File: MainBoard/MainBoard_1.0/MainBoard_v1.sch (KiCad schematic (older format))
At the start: 165 parts, among them J1 ILG, J10 SH, J11 SH, J12 SH, J13 FFC, J14 SH, J2 SH, J3 SH, J4 PA, J5 Micro_SD_Card_Det_Hirose_DM3AT, J6 SH, J7 ENC, J8 ENC, J9 PA, Q1 AON7400B, Q10 IRLML6344, Q2 AON7400B, Q3 AON7400B, Q4 AON7400B, Q5 AON7400B, Q6 AON7400B, Q7 2N7002K, Q8 AON7400B, Q9 AON7400B, SW1 SKRPACE010, SW2 SSSS213202, SW3 FR01SC16P-S, SW4 SKRHAAE010, U1 SI7469DP-T1-GE3, U10 DRV8701E, U11 MMC5983MA, U2 LT1963A-TSSOP, U3 TPS62143, U4 ECS-2520S33, U5 INA260, U6 DRV8701E, U7 ICM20648, U8 STM32F469VG, U9 INA260

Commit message: ver_2021
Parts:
- C2, C28, C44: symbol Device:CP_Small -> MainBoard_v1-rescue:CP_Small-Device
- D1, D7: symbol Device:D_Schottky_Small_ALT -> MainBoard_v1-rescue:D_Schottky_Small_ALT-Device
- D2, D3: symbol Device:D_Zener_Small_ALT -> MainBoard_v1-rescue:D_Zener_Small_ALT-Device
- D4, D5, D6, D8, D9: symbol Device:LED_Small_ALT -> MainBoard_v1-rescue:LED_Small_ALT-Device
- FB1, FB2, FB3, FB4, FB5, FB6, FB7: symbol Device:Ferrite_Bead_Small -> MainBoard_v1-rescue:Ferrite_Bead_Small-Device
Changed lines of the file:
@@
 $EndComp
 $Comp
-L Device:CP_Small C2
+L MainBoard_v1-rescue:CP_Small-Device C2
 U 1 1 5EC9A733
 P 7750 1700
@@
 	12850 1050 12850 1200
 $Comp
-L Device:D_Zener_Small_ALT D3
+L MainBoard_v1-rescue:D_Zener_Small_ALT-Device D3
 U 1 1 5ECD6403
 P 12600 1700
@@
 $EndComp
 $Comp
-L Device:D_Zener_Small_ALT D2
+L MainBoard_v1-rescue:D_Zener_Small_ALT-Device D2
 U 1 1 5ECD7671
 P 8900 1700
@@
 	8900 1800 8900 2150
 $Comp
-L Device:D_Schottky_Small_ALT D1
+L MainBoard_v1-rescue:D_Schottky_Small_ALT-Device D1
 U 1 1 5ECDC58D
 P 8750 1200
@@
 Connection ~ 1300 4500
 $Comp
-L Device:Ferrite_Bead_Small FB1
+L MainBoard_v1-rescue:Ferrite_Bead_Small-Device FB1
 U 1 1 5ECC6524
 P 1000 5700
@@
 $EndComp
 $Comp
-L Device:LED_Small_ALT D4
+L MainBoard_v1-rescue:LED_Small_ALT-Device D4
 U 1 1 5ECAB4EE
 P 8450 1850
@@
 $EndComp
 $Comp
-L Device:LED_Small_ALT D5
+L MainBoard_v1-rescue:LED_Small_ALT-Device D5
 U 1 1 5ECEEE7F
 P 12850 1850
@@
 $EndComp
 $Comp
-L Device:LED_Small_ALT D6
+L MainBoard_v1-rescue:LED_Small_ALT-Device D6
 U 1 1 5ED0949D
 P 15750 1850
@@
 Connection ~ 2000 8100
 $Comp
-L Device:D_Schottky_Small_ALT D7
+L MainBoard_v1-rescue:D_Schottky_Small_ALT-Device D7
 U 1 1 5F19FBEA
 P 1650 7400
@@
 	8550 6800 8550 7050
 $Comp
-L Device:Ferrite_Bead_Small FB2
+L MainBoard_v1-rescue:Ferrite_Bead_Small-Device FB2
 U 1 1 60318787
 P 6850 5900
@@
 $EndComp
 $Comp
-L Device:Ferrite_Bead_Small FB3
+L MainBoard_v1-rescue:Ferrite_Bead_Small-Device FB3
 U 1 1 60368094
 P 6850 6000
@@
 $EndComp
 $Comp
-L Device:Ferrite_Bead_Small FB4
+L MainBoard_v1-rescue:Ferrite_Bead_Small-Device FB4
 U 1 1 603B73FE
 P 6850 6100
@@
 $EndComp
 $Comp
-L Device:Ferrite_Bead_Small FB5
+L MainBoard_v1-rescue:Ferrite_Bead_Small-Device FB5
 U 1 1 60406759
 P 6850 6300
@@
 $EndComp
 $Comp
-L Device:Ferrite_Bead_Small FB6
+L MainBoard_v1-rescue:Ferrite_Bead_Small-Device FB6
 U 1 1 60455AD2
 P 6850 6500
@@
 $EndComp
 $Comp
-L Device:Ferrite_Bead_Small FB7
+L MainBoard_v1-rescue:Ferrite_Bead_Small-Device FB7
 U 1 1 604A4F68
 P 6850 6600
@@
 	9800 11000 10450 11000
 $Comp
-L Device:CP_Small C28
+L MainBoard_v1-rescue:CP_Small-Device C28
 U 1 1 67BA8F60
 P 14300 5400
@@
 	14300 5200 14300 5300
 $Comp
-L Device:CP_Small C44
+L MainBoard_v1-rescue:CP_Small-Device C44
 U 1 1 6806CE8E
 P 14150 9150
@@
 Wire Wire Line
 	6300 9200 6300 9250
-Text GLabel 6250 9900 0    50   Input ~ 0
-EXTRA1
 Text GLabel 6250 10000 0    50   Input ~ 0
+EXTRA1
+Text GLabel 6250 9900 0    50   Input ~ 0
 EXTRA2
 $Comp
@@
 	3400 10000 3400 10100
 $Comp
-L Device:LED_Small_ALT D8
+L MainBoard_v1-rescue:LED_Small_ALT-Device D8
 U 1 1 61039744
 P 1150 10550
@@
 $EndComp
 $Comp
-L Device:LED_Small_ALT D9
+L MainBoard_v1-rescue:LED_Small_ALT-Device D9
 U 1 1 6103974A
 P 1450 10550

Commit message: fixed right bottom
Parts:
- removed J3: SH, Connectors_JST:JST_SH_BM06B-SRSS-TB_06x1.00mm_Straight, symbol Connector_Generic:Conn_01x06
- added J3: STDC14, Connector_PinHeader_1.27mm:PinHeader_2x07_P1.27mm_Vertical_SMD, symbol Connector_Generic:Conn_02x07_Odd_Even
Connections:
- net +3V3: now also J3.3 (Pin_3)
- net ESC1_PWM: now also U8.99 (PB9); no longer U8.94 (PB5)
- net ESC2_PWM: now also U8.98 (PB8); no longer U8.93 (PB4)
- net ESC3_PWM: now also U8.94 (PB5); no longer U8.98 (PB8)
- net ESC4_PWM: now also U8.93 (PB4); no longer U8.99 (PB9)
- net GND: now also U7.11 (FSYNC), J3.11 (Pin_11), J3.5 (Pin_5), J3.7 (Pin_7)
- net NRST: now also J3.12 (Pin_12)
- net R_SW1: now also U8.85 (PD1); no longer U8.35 (PE10)
- net R_SW2: now also U8.87 (PD3); no longer U8.33 (PE8)
- net R_SW4: now also U8.88 (PD4); no longer U8.32 (PE7)
- net R_SW8: now also U8.91 (PD7); no longer U8.31 (PB2)
- net SW1: now also U8.31 (PB2); no longer U8.91 (PD7)
- net SW2: now also U8.32 (PE7); no longer U8.88 (PD4)
- net SW3: now also U8.33 (PE8); no longer U8.87 (PD3)
- net SW4: now also U8.35 (PE10); no longer U8.85 (PD1)
- net SWCLK: now also J3.6 (Pin_6)
- net SWDIO: now also J3.4 (Pin_4)
- net SWO: now also J3.8 (Pin_8)
- no-connect marks 46 -> 51
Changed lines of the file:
@@
 $EndComp
 $Comp
-L MainBoard_v1-rescue:ICM20648-shimoharu_library U7
-U 1 1 5EC2BB3D
-P 7750 4450
-F 0 "U7" V 8900 3400 50  0000 L CNN
-F 1 "ICM20648" V 8800 3150 50  0000 L CNN
-F 2 "Footprint:ICM20648" H 7750 4450 50  0001 C CNN
-F 3 "" H 7750 4450 50  0001 C CNN
-	1    7750 4450
-	0    -1   -1   0
-$EndComp
-$Comp
 L Connector_Generic:Conn_01x02 J1
 U 1 1 5EC51A22
@@
 Wire Wire Line
 	1300 4700 2050 4700
-Text GLabel 3050 6900 3    50   Input ~ 0
+Text GLabel 3450 3500 1    50   Input ~ 0
 R_SW8
-Text GLabel 3150 6900 3    50   Input ~ 0
+Text GLabel 3750 3500 1    50   Input ~ 0
 R_SW4
-Text GLabel 3250 6900 3    50   Input ~ 0
+Text GLabel 3850 3500 1    50   Input ~ 0
 R_SW2
-Text GLabel 3450 6900 3    50   Input ~ 0
+Text GLabel 4050 3500 1    50   Input ~ 0
 R_SW1
 Text GLabel 2050 5100 0    50   Input ~ 0
@@
 Text GLabel 4150 3500 1    50   Input ~ 0
 SW5
-Text GLabel 4050 3500 1    50   Input ~ 0
+Text GLabel 3450 6900 3    50   Input ~ 0
 SW4
-Text GLabel 3850 3500 1    50   Input ~ 0
+Text GLabel 3250 6900 3    50   Input ~ 0
 SW3
-Text GLabel 3750 3500 1    50   Input ~ 0
+Text GLabel 3150 6900 3    50   Input ~ 0
 SW2
 Text GLabel 3650 3500 1    50   Input ~ 0
@@
 Text GLabel 3550 3500 1    50   Input ~ 0
 USART_RX
-Text GLabel 3450 3500 1    50   Input ~ 0
+Text GLabel 3050 6900 3    50   Input ~ 0
 SW1
-Text GLabel 3150 3500 1    50   Input ~ 0
+Text GLabel 2650 3500 1    50   Input ~ 0
 ESC1_PWM
-Text GLabel 3250 3500 1    50   Input ~ 0
+Text GLabel 2750 3500 1    50   Input ~ 0
 ESC2_PWM
 Text GLabel 3050 3500 1    50   Input ~ 0
@@
 Wire Wire Line
 	2850 2900 2850 3500
-Text GLabel 2750 3500 1    50   Input ~ 0
-ESC3_PWM
-Text GLabel 2650 3500 1    50   Input ~ 0
+Text GLabel 3250 3500 1    50   Input ~ 0
 ESC4_PWM
+Text GLabel 3150 3500 1    50   Input ~ 0
+ESC3_PWM
 Text GLabel 3950 6900 3    50   Input ~ 0
 EXTRA2
@@
 Connection ~ 3150 1900
 $Comp
-L Connector_Generic:Conn_01x06 J3
-U 1 1 5ED71E7C
-P 4800 1350
-F 0 "J3" H 4880 1342 50  0000 L CNN
-F 1 "SH" H 4880 1251 50  0000 L CNN
-F 2 "Connectors_JST:JST_SH_BM06B-SRSS-TB_06x1.00mm_Straight" H 4800 1350 50  0001 C CNN
-F 3 "~" H 4800 1350 50  0001 C CNN
-	1    4800 1350
-	1    0    0    -1
-$EndComp
-$Comp
 L Connector_Generic:Conn_01x04 J2
 U 1 1 5ED7299E
@@
 L power:+3.3V #PWR03
 U 1 1 5ED95FDD
-P 4600 850
-F 0 "#PWR03" H 4600 700 50  0001 C CNN
-F 1 "+3.3V" H 4615 1023 50  0000 C CNN
-F 2 "" H 4600 850 50  0001 C CNN
-F 3 "" H 4600 850 50  0001 C CNN
-	1    4600 850
+P 4300 950
+F 0 "#PWR03" H 4300 800 50  0001 C CNN
+F 1 "+3.3V" H 4315 1123 50  0000 C CNN
+F 2 "" H 4300 950 50  0001 C CNN
+F 3 "" H 4300 950 50  0001 C CNN
+	1    4300 950
 	-1   0    0    -1
 $EndComp
 Wire Wire Line
-	4600 850  4600 1150
+	4300 950  4300 1250
 $Comp
 L power:GND #PWR010
 U 1 1 5EDA1506
-P 4200 2050
-F 0 "#PWR010" H 4200 1800 50  0001 C CNN
-F 1 "GND" H 4205 1877 50  0000 C CNN
-F 2 "" H 4200 2050 50  0001 C CNN
-F 3 "" H 4200 2050 50  0001 C CNN
-	1    4200 2050
+P 4100 1750
+F 0 "#PWR010" H 4100 1500 50  0001 C CNN
+F 1 "GND" H 4105 1577 50  0000 C CNN
+F 2 "" H 4100 1750 50  0001 C CNN
+F 3 "" H 4100 1750 50  0001 C CNN
+	1    4100 1750
 	1    0    0    -1
 $EndComp
-Wire Wire Line
-	4200 2050 4200 1350
 $Comp
 L power:+3.3V #PWR04
@@
 Wire Wire Line
 	5750 2000 5750 1450
-Text GLabel 4600 1250 0    50   Input ~ 0
-SWCLK
-Text GLabel 4600 1450 0    50   Input ~ 0
+Text GLabel 4950 1250 2    50   Input ~ 0
 SWDIO
-Text GLabel 4600 1550 0    50   Input ~ 0
+Text GLabel 4950 1650 2    50   Input ~ 0
 NRST
-Text GLabel 4600 1650 0    50   Input ~ 0
+Text GLabel 4950 1450 2    50   Input ~ 0
 SWO
-Wire Wire Line
-	4200 1350 4600 1350
 Text GLabel 5750 1250 0    50   Input ~ 0
 USART_RX
@@
 	7150 3800 7150 3050
 NoConn ~ 8850 3700
-NoConn ~ 8850 3800
 NoConn ~ 7950 3200
 NoConn ~ 8050 3200
@@
 	7500 4300 7500 4800
 Wire Wire Line
-	7500 4800 8900 4800
-Wire Wire Line
 	8900 4800 8900 4000
 Wire Wire Line
@@
 Wire Wire Line
 	6600 4300 7500 4300
+Wire Wire Line
+	7500 4800 8900 4800
+$Comp
+L MainBoard_v1-rescue:ICM20648-shimoharu_library U7
+U 1 1 5EC2BB3D
+P 7750 4450
+F 0 "U7" V 8900 3400 50  0000 L CNN
+F 1 "ICM20648" V 8800 3150 50  0000 L CNN
+F 2 "Footprint:ICM20648" H 7750 4450 50  0001 C CNN
+F 3 "" H 7750 4450 50  0001 C CNN
+	1    7750 4450
+	0    -1   -1   0
+$EndComp
+Wire Wire Line
+	8850 3800 9400 3800
+Wire Wire Line
+	9400 3800 9400 3900
+Connection ~ 9400 3900
+Text GLabel 4950 1350 2    50   Input ~ 0
+SWCLK
+NoConn ~ 4450 1150
+NoConn ~ 4950 1150
+Wire Wire Line
+	4300 1250 4450 1250
+Wire Wire Line
+	4100 1750 4100 1650
+Wire Wire Line
+	4100 1350 4450 1350
+$Comp
+L Connector_Generic:Conn_02x07_Odd_Even J3
+U 1 1 60D502E8
+P 4650 1450
+F 0 "J3" H 4700 1967 50  0000 C CNN
+F 1 "STDC14" H 4700 1876 50  0000 C CNN
+F 2 "Connector_PinHeader_1.27mm:PinHeader_2x07_P1.27mm_Vertical_SMD" H 4650 1450 50  0001 C CNN
+F 3 "~" H 4650 1450 50  0001 C CNN
+	1    4650 1450
+	1    0    0    -1
+$EndComp
+Wire Wire Line
+	4450 1450 4100 1450
+Connection ~ 4100 1450
+Wire Wire Line
+	4100 1450 4100 1350
+NoConn ~ 4450 1550
+NoConn ~ 4950 1550
+Wire Wire Line
+	4450 1650 4100 1650
+Connection ~ 4100 1650
+Wire Wire Line
+	4100 1650 4100 1450
+NoConn ~ 4450 1750
+NoConn ~ 4950 1750
 $EndSCHEMATC

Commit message: wiring completed
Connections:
- net SW1: now also U8.35 (PE10); no longer U8.31 (PB2)
- net SW2: now also U8.84 (PD0); no longer U8.32 (PE7)
- net SW4: now also U8.31 (PB2); no longer U8.35 (PE10)
- net SW5: now also U8.32 (PE7); no longer U8.84 (PD0)
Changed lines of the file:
@@
 Text GLabel 4550 3500 1    50   Input ~ 0
 SD_INSERT
-Text GLabel 4150 3500 1    50   Input ~ 0
+Text GLabel 3150 6900 3    50   Input ~ 0
 SW5
-Text GLabel 3450 6900 3    50   Input ~ 0
+Text GLabel 3050 6900 3    50   Input ~ 0
 SW4
 Text GLabel 3250 6900 3    50   Input ~ 0
 SW3
-Text GLabel 3150 6900 3    50   Input ~ 0
+Text GLabel 4150 3500 1    50   Input ~ 0
 SW2
 Text GLabel 3650 3500 1    50   Input ~ 0
@@
 Text GLabel 3550 3500 1    50   Input ~ 0
 USART_RX
-Text GLabel 3050 6900 3    50   Input ~ 0
+Text GLabel 3450 6900 3    50   Input ~ 0
 SW1
 Text GLabel 2650 3500 1    50   Input ~ 0

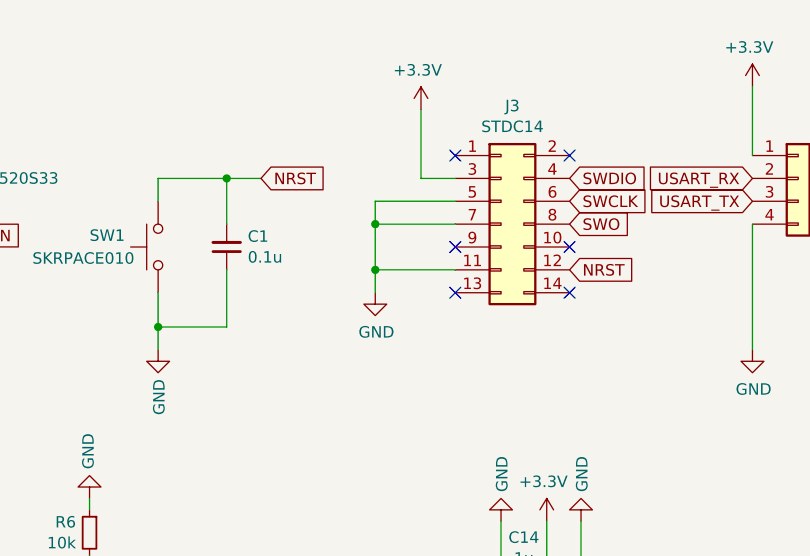
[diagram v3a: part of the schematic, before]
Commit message: remove antena and move referencse by main board
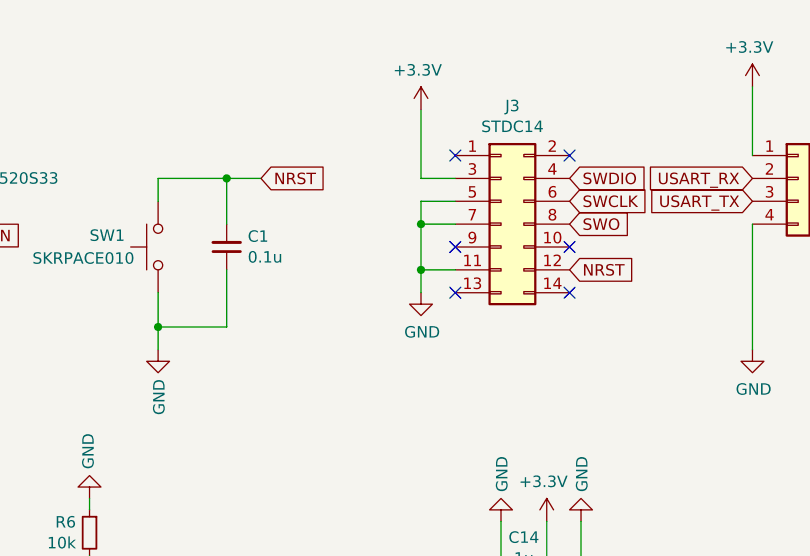
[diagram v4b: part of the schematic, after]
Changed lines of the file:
@@
 L power:GND #PWR010
 U 1 1 5EDA1506
-P 4100 1750
-F 0 "#PWR010" H 4100 1500 50  0001 C CNN
-F 1 "GND" H 4105 1577 50  0000 C CNN
-F 2 "" H 4100 1750 50  0001 C CNN
-F 3 "" H 4100 1750 50  0001 C CNN
-	1    4100 1750
+P 4300 1750
+F 0 "#PWR010" H 4300 1500 50  0001 C CNN
+F 1 "GND" H 4305 1577 50  0000 C CNN
+F 2 "" H 4300 1750 50  0001 C CNN
+F 3 "" H 4300 1750 50  0001 C CNN
+	1    4300 1750
 	1    0    0    -1
 $EndComp
@@
 	4300 1250 4450 1250
 Wire Wire Line
-	4100 1750 4100 1650
+	4300 1750 4300 1650
 Wire Wire Line
-	4100 1350 4450 1350
+	4300 1350 4450 1350
 $Comp
 L Connector_Generic:Conn_02x07_Odd_Even J3
@@
 $EndComp
 Wire Wire Line
-	4450 1450 4100 1450
-Connection ~ 4100 1450
+	4450 1450 4300 1450
+Connection ~ 4300 1450
 Wire Wire Line
-	4100 1450 4100 1350
+	4300 1450 4300 1350
 NoConn ~ 4450 1550
 NoConn ~ 4950 1550
 Wire Wire Line
-	4450 1650 4100 1650
-Connection ~ 4100 1650
+	4450 1650 4300 1650
+Connection ~ 4300 1650
 Wire Wire Line
-	4100 1650 4100 1450
+	4300 1650 4300 1450
 NoConn ~ 4450 1750
 NoConn ~ 4950 1750

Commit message: change capaciter size
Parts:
- C2: footprint Capacitors_SMD:CP_Elec_5x5.8 -> Capacitor_SMD:CP_Elec_6.3x5.9
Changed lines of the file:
@@
 F 0 "C2" H 7838 1746 50  0000 L CNN
 F 1 "100u" H 7838 1655 50  0000 L CNN
-F 2 "Capacitors_SMD:CP_Elec_5x5.8" H 7750 1700 50  0001 C CNN
+F 2 "Capacitor_SMD:CP_Elec_6.3x5.9" H 7750 1700 50  0001 C CNN
 F 3 "~" H 7750 1700 50  0001 C CNN
 	1    7750 1700
